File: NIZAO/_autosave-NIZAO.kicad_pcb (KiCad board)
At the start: 4 copper layers, 102 x 82.8 mm, 180 parts, among them J1 Screw_Terminal_01x09, J2 Screw_Terminal_01x09, J3 Screw_Terminal_01x09, J4 Screw_Terminal_01x09, J5 PZ254R-12-14P, K1 G5V-1, K2 G5V-1, Q1 NCE60P04R, Q2 ZXMS6004FFQTA, Q3 ZXMS6004FFQTA, Q4 ZXMS6004FFQTA, Q5 ZXMS6004FFQTA, SW1 TS-1088-AR02016, U1 ADS1115IDGS, U10 AT3H4B-CUH-S, U11 MAX31856MUD+, U12 BL0942, U13 B0303S-1WR3_C7465185, U14 ISO7021DR, U15 GP8211S-TC50-EW, U16 GP8302-TC50-EW, U17 BTS723GWXUMA1, U18 LK1802, U2 ESP32-S3-WROOM-1, U3 RS485-PROTECT, U4 AP63203WU, U5 AT3H4B-CUH-S, U6 AT3H4B-CUH-S, U7 AT3H4B-CUH-S, U8 AT3H4B-CUH-S, U9 AT3H4B-CUH-S

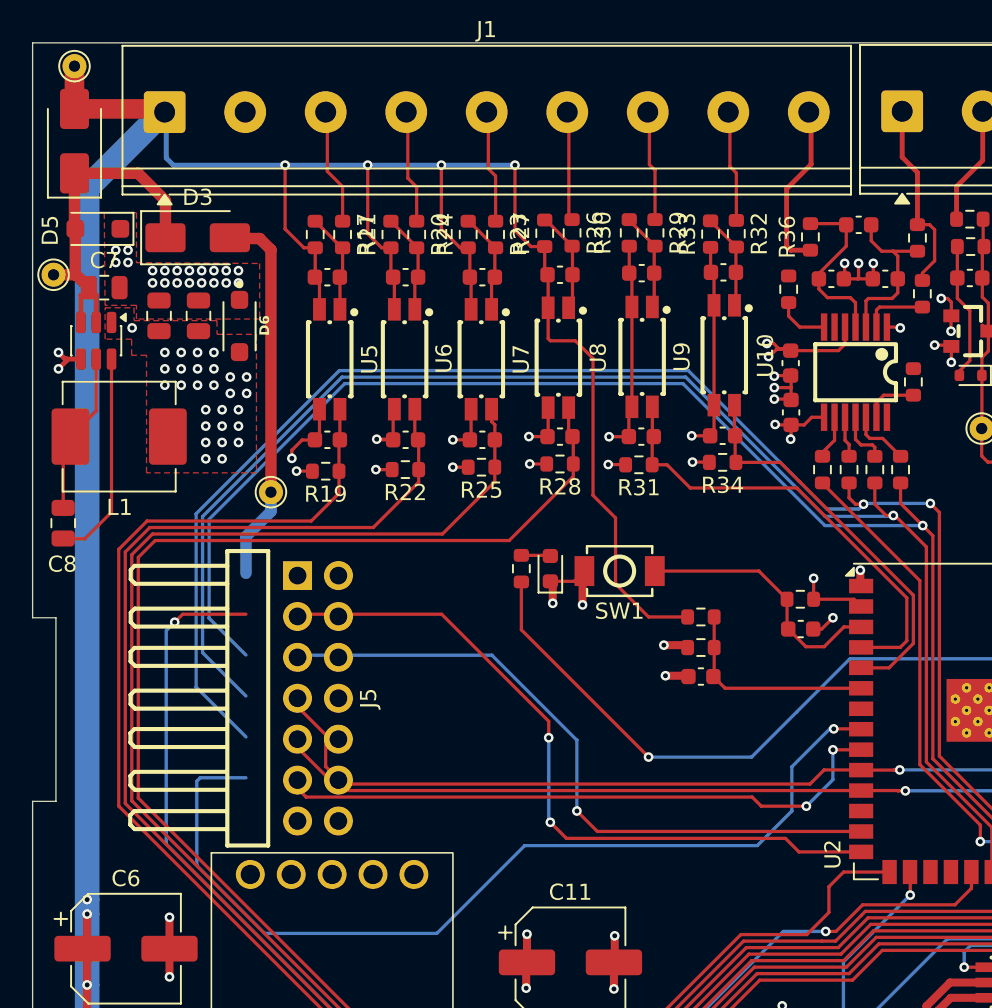
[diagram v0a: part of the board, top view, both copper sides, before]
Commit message: Actualiza el mezzanine, eliminar assembly de prueba y actualizar essembly
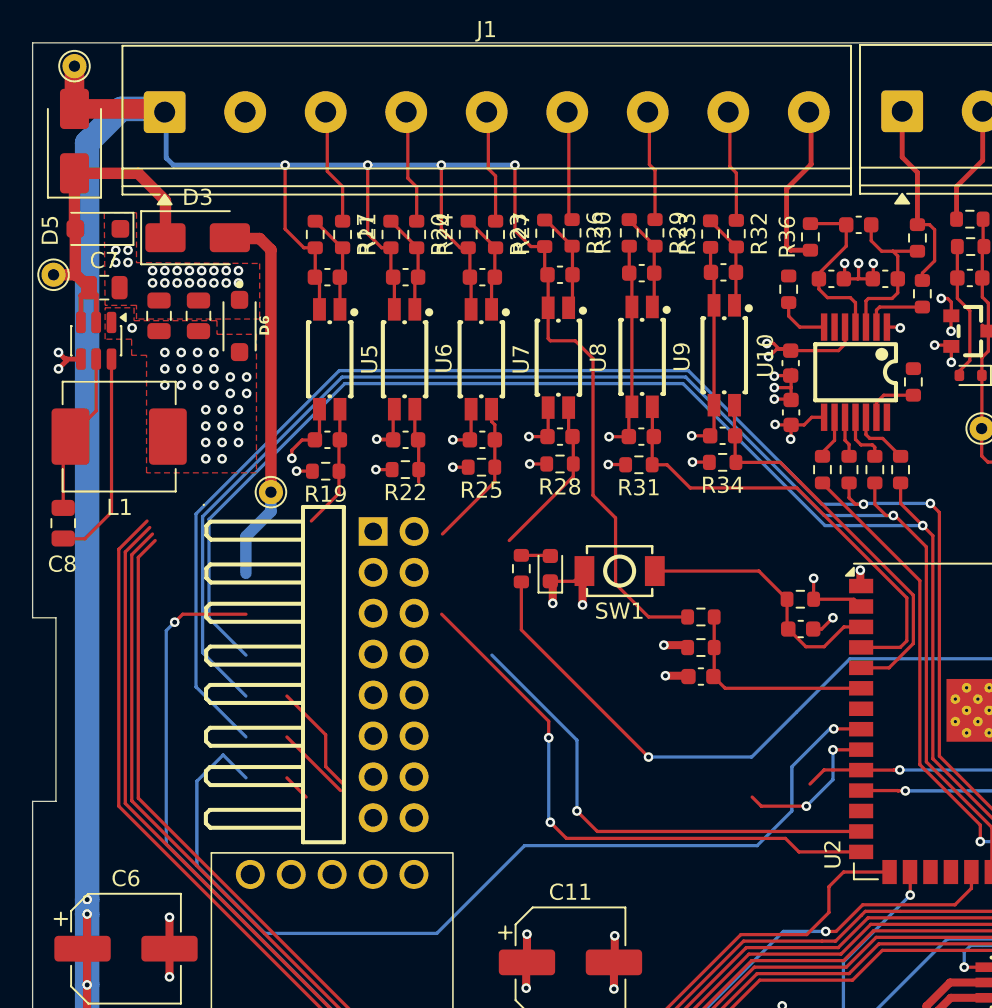
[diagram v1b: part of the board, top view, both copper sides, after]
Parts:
- removed J5: PZ254R-12-14P, XFCN PZ254R-12-14P:HDR-TH_14P-P2.54-H-M-R2-C7-S2.54
- added H3: PZ254R-12-16P, EasyEDA:HDR-TH_16P-P2.54-H-M-R2-C8-S2.54, F.Cu at (122.9, 94.7)
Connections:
- C17 pad 1: Net-(C17-Pad1) -> Net-(U19-AN/CAT)
- C19 pad 1: Net-(C19-Pad1) -> Net-(U20-AN/CAT)
- C21 pad 1: Net-(C21-Pad1) -> Net-(U21-AN/CAT)
- C23 pad 1: Net-(C23-Pad1) -> Net-(U22-AN/CAT)
- C25 pad 1: Net-(C25-Pad1) -> Net-(U23-AN/CAT)
- C27 pad 1: Net-(C27-Pad1) -> Net-(U24-AN/CAT)
- R17 pad 2: Net-(C17-Pad1) -> Net-(U19-AN/CAT)
- R18 pad 2: Net-(C17-Pad1) -> Net-(U19-AN/CAT)
- R20 pad 2: Net-(C19-Pad1) -> Net-(U20-AN/CAT)
- R21 pad 2: Net-(C19-Pad1) -> Net-(U20-AN/CAT)
- R23 pad 2: Net-(C21-Pad1) -> Net-(U21-AN/CAT)
- R24 pad 2: Net-(C21-Pad1) -> Net-(U21-AN/CAT)
- R26 pad 2: Net-(C23-Pad1) -> Net-(U22-AN/CAT)
- R27 pad 2: Net-(C23-Pad1) -> Net-(U22-AN/CAT)
- R29 pad 2: Net-(C25-Pad1) -> Net-(U23-AN/CAT)
- R30 pad 2: Net-(C25-Pad1) -> Net-(U23-AN/CAT)
- R32 pad 2: Net-(C27-Pad1) -> Net-(U24-AN/CAT)
- R33 pad 2: Net-(C27-Pad1) -> Net-(U24-AN/CAT)
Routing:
- net /BoardNIZAO/i2c_scl: track 120.9 -> 88.6 mm
- net /BoardNIZAO/i2c_sda: track 122.0 -> 93.1 mm
- net /BoardNIZAO/GPIO2: track 38.9 -> 11.2 mm
- net /BoardNIZAO/IN_NPN4: track 106.5 -> 84.5 mm
- net /BoardNIZAO/IN_NPN3: track 143.2 -> 125.1 mm
- net /BoardNIZAO/IN_NPN2: track 142.1 -> 124.2 mm
- net /BoardNIZAO/usb-: track 42.8 -> 30.0 mm
- net /BoardNIZAO/IN_NPN1: track 117.4 -> 107.2 mm
- net /BoardNIZAO/usb+: track 45.4 -> 35.8 mm
- net +24V: track 354.0 -> 355.6 mm
- net /BoardNIZAO/GPIO1: track 58.2 -> 59.4 mm
